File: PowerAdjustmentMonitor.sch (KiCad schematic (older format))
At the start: 37 parts, among them U3 LM317T, U4 LM317T, U5 LM337T, U6 LM337T

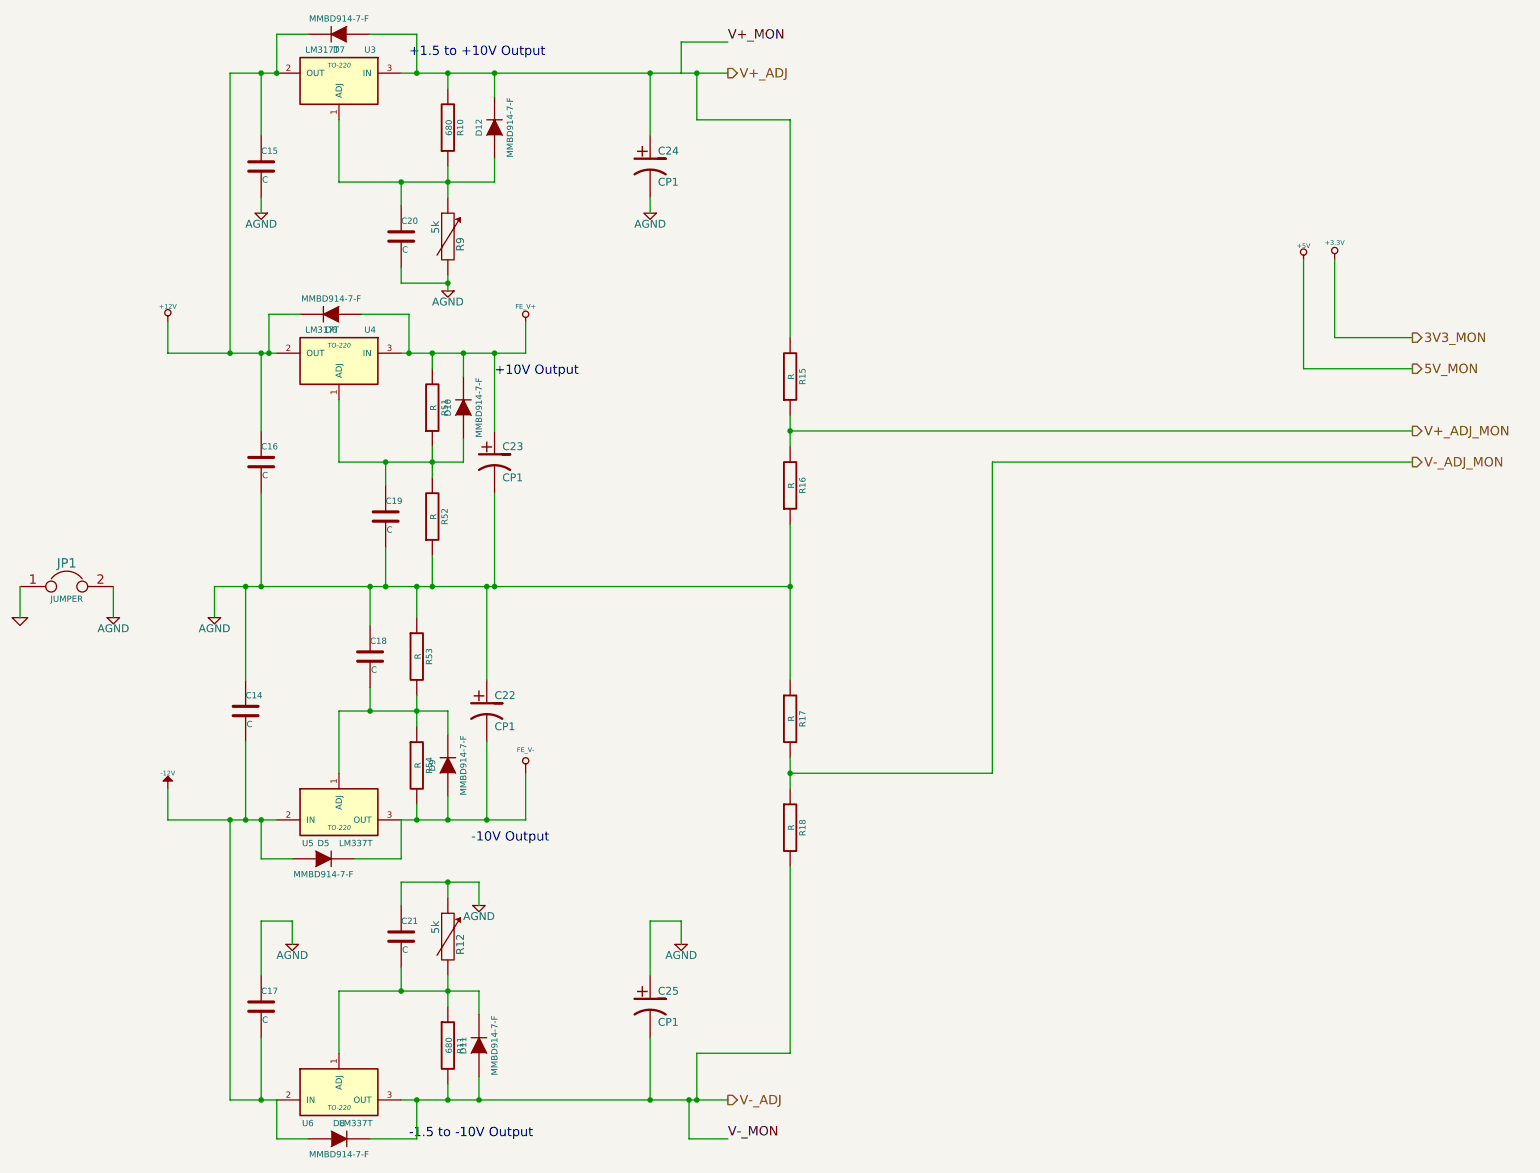
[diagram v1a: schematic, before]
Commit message: Updates from Layout Work Session 4 video
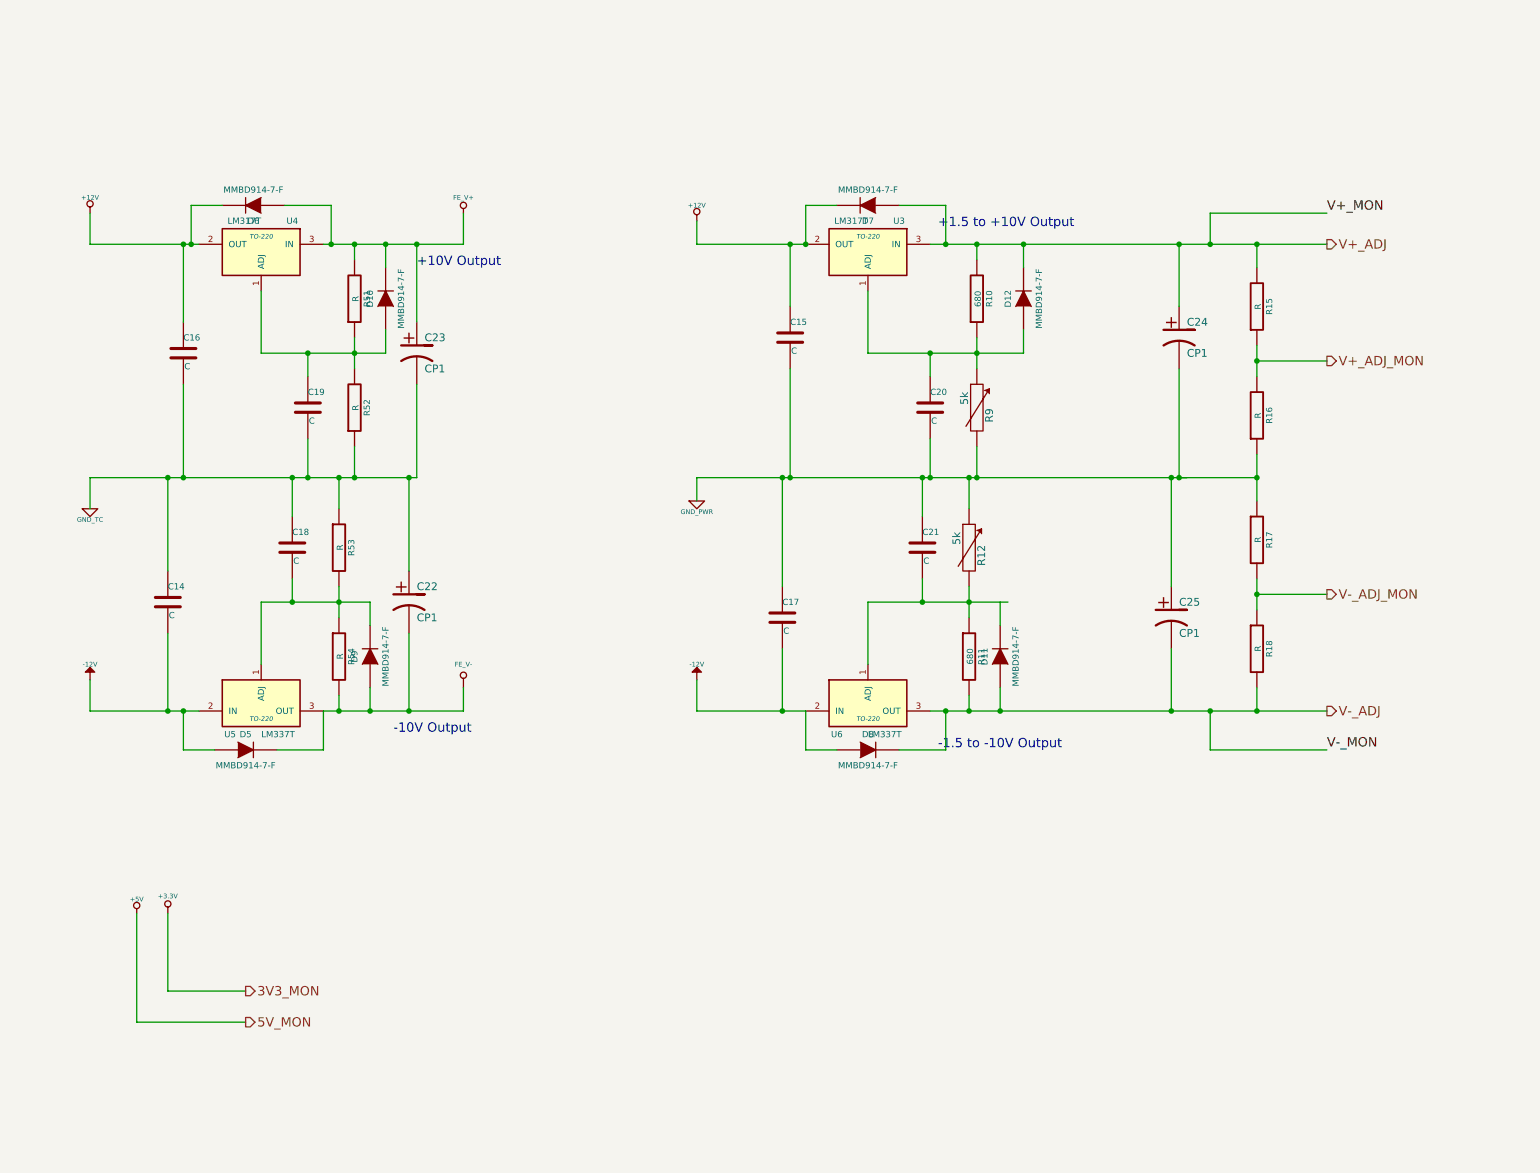
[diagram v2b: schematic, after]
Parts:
- removed JP1: JUMPER, symbol JUMPER
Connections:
- net at C21.2, R11.1, R12.2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: no longer D11.2 (K)
- net AGND renamed GND_PWR
- net GND_PWR: no longer C14.1, C16.2, C18.1, C19.2, C22.1, C23.2, R52.1, R53.1
- new net GND_TC: C14.1, C16.2, C18.1, C19.2, C22.1, C23.2, R52.1, R53.1
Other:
- moved on the sheet: C14, C15, C16, C17, C18, C19, C20, C21, C22, C23, C24, C25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

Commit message: Updates from Layout Work Session 5 video
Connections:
- net GND_TC renamed AGND
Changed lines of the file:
@@
 $EndDescr
 $Comp
-L +3.3V #PWR024
+L +3.3V #PWR025
 U 1 1 52F2A379
 P 2200 6200
-F 0 "#PWR024" H 2200 6160 30  0001 C CNN
+F 0 "#PWR025" H 2200 6160 30  0001 C CNN
 F 1 "+3.3V" H 2200 6310 30  0000 C CNN
 F 2 "" H 2200 6200 60  0000 C CNN
@@
 $EndComp
 $Comp
-L +5V #PWR025
+L +5V #PWR026
 U 1 1 52F2A37F
 P 2000 6200
-F 0 "#PWR025" H 2000 6290 20  0001 C CNN
+F 0 "#PWR026" H 2000 6290 20  0001 C CNN
 F 1 "+5V" H 2000 6290 30  0000 C CNN
 F 2 "" H 2000 6200 60  0000 C CNN
@@
 $EndComp
 $Comp
-L +12V #PWR026
+L +12V #PWR027
 U 1 1 52F2A40B
 P 1700 1700
-F 0 "#PWR026" H 1700 1650 20  0001 C CNN
+F 0 "#PWR027" H 1700 1650 20  0001 C CNN
 F 1 "+12V" H 1700 1800 30  0000 C CNN
 F 2 "" H 1700 1700 60  0000 C CNN
@@
 $EndComp
 $Comp
-L -12V #PWR027
+L -12V #PWR028
 U 1 1 52F2A411
 P 1700 4700
-F 0 "#PWR027" H 1700 4830 20  0001 C CNN
+F 0 "#PWR028" H 1700 4830 20  0001 C CNN
 F 1 "-12V" H 1700 4800 30  0000 C CNN
 F 2 "" H 1700 4700 60  0000 C CNN
@@
 $EndComp
 $Comp
-L FE_V+ #PWR028
+L FE_V+ #PWR029
 U 1 1 52F2A802
 P 4100 1700
-F 0 "#PWR028" H 4100 1800 30  0001 C CNN
+F 0 "#PWR029" H 4100 1800 30  0001 C CNN
 F 1 "FE_V+" H 4100 1800 30  0000 C CNN
 F 2 "" H 4100 1700 60  0000 C CNN
@@
 $EndComp
 $Comp
-L GND_PWR #PWR029
+L GND_PWR #PWR030
 U 1 1 53152874
 P 5600 3550
-F 0 "#PWR029" H 5600 3550 30  0001 C CNN
+F 0 "#PWR030" H 5600 3550 30  0001 C CNN
 F 1 "GND_PWR" H 5600 3480 30  0000 C CNN
 F 2 "" H 5600 3550 60  0000 C CNN
@@
 $EndComp
 $Comp
-L +12V #PWR030
+L +12V #PWR031
 U 1 1 5315289E
 P 5600 1750
-F 0 "#PWR030" H 5600 1700 20  0001 C CNN
+F 0 "#PWR031" H 5600 1700 20  0001 C CNN
 F 1 "+12V" H 5600 1850 30  0000 C CNN
 F 2 "" H 5600 1750 60  0000 C CNN
@@
 $EndComp
 $Comp
-L -12V #PWR031
+L -12V #PWR032
 U 1 1 53152B82
 P 5600 4700
-F 0 "#PWR031" H 5600 4830 20  0001 C CNN
+F 0 "#PWR032" H 5600 4830 20  0001 C CNN
 F 1 "-12V" H 5600 4800 30  0000 C CNN
 F 2 "" H 5600 4700 60  0000 C CNN
@@
 	1    0    0    -1
 $EndComp
-$Comp
-L GND_TC #PWR032
-U 1 1 53152BBD
-P 1700 3600
-F 0 "#PWR032" H 1700 3600 30  0001 C CNN
-F 1 "GND_TC" H 1700 3530 30  0000 C CNN
-F 2 "" H 1700 3600 60  0000 C CNN
-F 3 "" H 1700 3600 60  0000 C CNN
-	1    1700 3600
-	1    0    0    -1
-$EndComp
 Wire Wire Line
 	1700 4900 1700 4700
@@
 	3200 5150 3200 4900
 Wire Wire Line
-	2300 4900 2300 5150
+	2300 5150 2300 4900
 Connection ~ 2300 4900
 Wire Wire Line
@@
 	8700 3400 8700 2700
 Connection ~ 8700 3400
+$Comp
+L AGND #PWR033
+U 1 1 5316392A
+P 1700 3600
+F 0 "#PWR033" H 1700 3600 40  0001 C CNN
+F 1 "AGND" H 1700 3530 50  0000 C CNN
+F 2 "" H 1700 3600 60  0000 C CNN
+F 3 "" H 1700 3600 60  0000 C CNN
+	1    1700 3600
+	1    0    0    -1
+$EndComp
 $EndSCHEMATC

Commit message: Updates from Layout Work Session 6 video
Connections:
- net at C21.2, R11.1, R12.2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: now also D11.2 (K)
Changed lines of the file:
@@
 $EndDescr
 $Comp
-L +3.3V #PWR025
+L +3.3V #PWR028
 U 1 1 52F2A379
 P 2200 6200
-F 0 "#PWR025" H 2200 6160 30  0001 C CNN
+F 0 "#PWR028" H 2200 6160 30  0001 C CNN
 F 1 "+3.3V" H 2200 6310 30  0000 C CNN
 F 2 "" H 2200 6200 60  0000 C CNN
@@
 $EndComp
 $Comp
-L +5V #PWR026
+L +5V #PWR029
 U 1 1 52F2A37F
 P 2000 6200
-F 0 "#PWR026" H 2000 6290 20  0001 C CNN
+F 0 "#PWR029" H 2000 6290 20  0001 C CNN
 F 1 "+5V" H 2000 6290 30  0000 C CNN
 F 2 "" H 2000 6200 60  0000 C CNN
@@
 $EndComp
 $Comp
-L +12V #PWR027
+L +12V #PWR030
 U 1 1 52F2A40B
 P 1700 1700
-F 0 "#PWR027" H 1700 1650 20  0001 C CNN
+F 0 "#PWR030" H 1700 1650 20  0001 C CNN
 F 1 "+12V" H 1700 1800 30  0000 C CNN
 F 2 "" H 1700 1700 60  0000 C CNN
@@
 $EndComp
 $Comp
-L -12V #PWR028
+L -12V #PWR031
 U 1 1 52F2A411
 P 1700 4700
-F 0 "#PWR028" H 1700 4830 20  0001 C CNN
+F 0 "#PWR031" H 1700 4830 20  0001 C CNN
 F 1 "-12V" H 1700 4800 30  0000 C CNN
 F 2 "" H 1700 4700 60  0000 C CNN
@@
 $EndComp
 $Comp
-L FE_V+ #PWR029
+L FE_V+ #PWR032
 U 1 1 52F2A802
 P 4100 1700
-F 0 "#PWR029" H 4100 1800 30  0001 C CNN
+F 0 "#PWR032" H 4100 1800 30  0001 C CNN
 F 1 "FE_V+" H 4100 1800 30  0000 C CNN
 F 2 "" H 4100 1700 60  0000 C CNN
@@
 $EndComp
 $Comp
-L FE_V- #PWR36
+L FE_V- #PWR37
 U 1 1 530BD9FD
 P 4100 4750
-F 0 "#PWR36" H 4100 4950 40  0001 C CNN
+F 0 "#PWR37" H 4100 4950 40  0001 C CNN
 F 1 "FE_V-" H 4100 4900 30  0000 C CNN
 F 2 "" H 4100 4750 60  0000 C CNN
@@
 $EndComp
 $Comp
-L GND_PWR #PWR030
+L GND_PWR #PWR033
 U 1 1 53152874
 P 5600 3550
-F 0 "#PWR030" H 5600 3550 30  0001 C CNN
+F 0 "#PWR033" H 5600 3550 30  0001 C CNN
 F 1 "GND_PWR" H 5600 3480 30  0000 C CNN
 F 2 "" H 5600 3550 60  0000 C CNN
@@
 $EndComp
 $Comp
-L +12V #PWR031
+L +12V #PWR034
 U 1 1 5315289E
 P 5600 1750
-F 0 "#PWR031" H 5600 1700 20  0001 C CNN
+F 0 "#PWR034" H 5600 1700 20  0001 C CNN
 F 1 "+12V" H 5600 1850 30  0000 C CNN
 F 2 "" H 5600 1750 60  0000 C CNN
@@
 $EndComp
 $Comp
-L -12V #PWR032
+L -12V #PWR035
 U 1 1 53152B82
 P 5600 4700
-F 0 "#PWR032" H 5600 4830 20  0001 C CNN
+F 0 "#PWR035" H 5600 4830 20  0001 C CNN
 F 1 "-12V" H 5600 4800 30  0000 C CNN
 F 2 "" H 5600 4700 60  0000 C CNN
@@
 	1700 3400 1700 3600
 Wire Wire Line
-	6700 4200 7600 4200
-Wire Wire Line
 	6700 4200 6700 4600
 Connection ~ 7350 4200
@@
 Connection ~ 8700 3400
 $Comp
-L AGND #PWR033
+L AGND #PWR036
 U 1 1 5316392A
 P 1700 3600
-F 0 "#PWR033" H 1700 3600 40  0001 C CNN
+F 0 "#PWR036" H 1700 3600 40  0001 C CNN
 F 1 "AGND" H 1700 3530 50  0000 C CNN
 F 2 "" H 1700 3600 60  0000 C CNN
@@
 	1    0    0    -1
 $EndComp
+Wire Wire Line
+	6700 4200 7550 4200
 $EndSCHEMATC

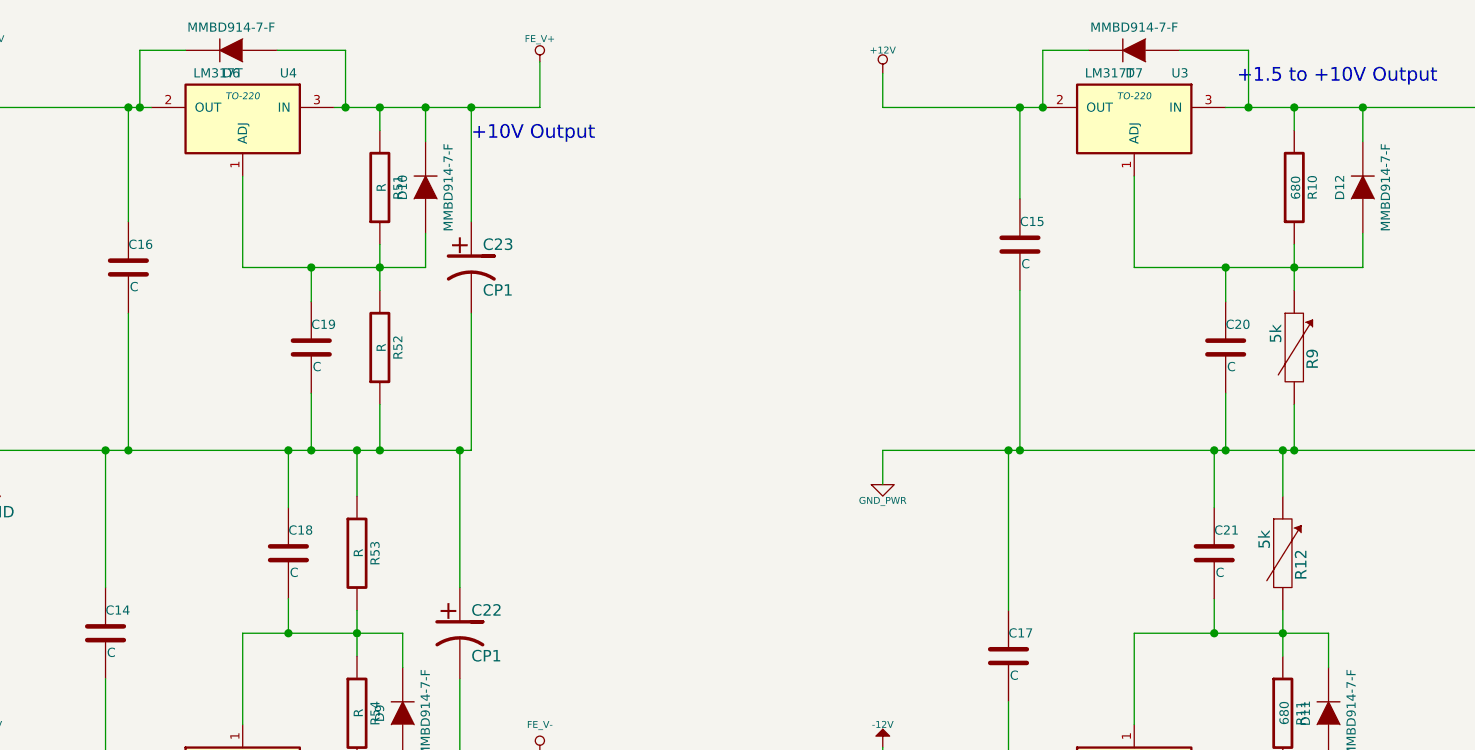
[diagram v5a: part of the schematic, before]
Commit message: Power output layout
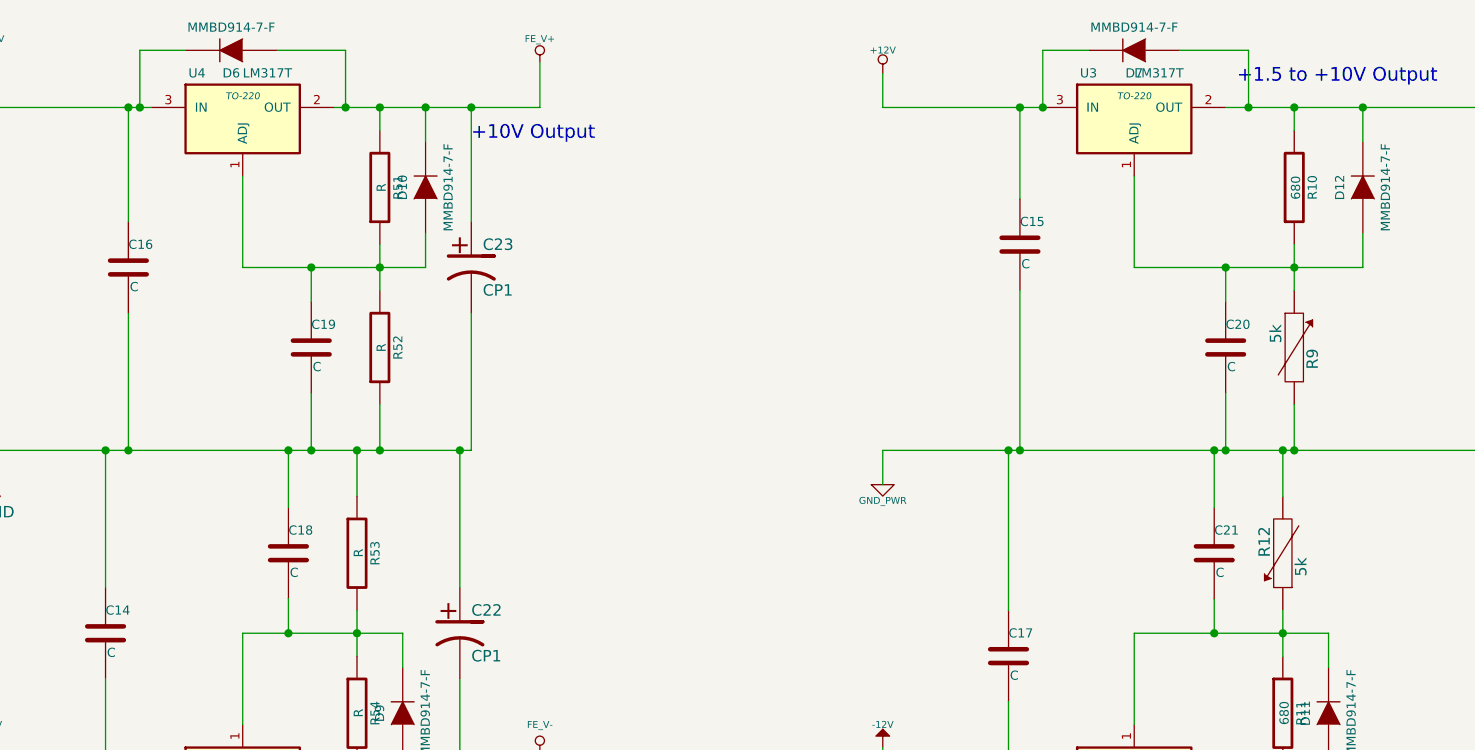
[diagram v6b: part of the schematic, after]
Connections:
- net +12V: now also U3.3 (IN), U4.3 (IN); no longer U3.2 (OUT), U4.2 (OUT)
- net FE_V+: now also U4.2 (OUT); no longer U4.3 (IN)
- net GND_PWR: now also R12.2; no longer R12.1
- net V+_ADJ: now also U3.2 (OUT); no longer U3.3 (IN)
- net at C21.2, D11.2 (K), R11.1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: now also R12.1; no longer R12.2
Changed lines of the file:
@@
 $EndDescr
 $Comp
-L +3.3V #PWR35
+L +3.3V #PWR027
 U 1 1 52F2A379
 P 2200 6200
-F 0 "#PWR35" H 2200 6160 30  0001 C CNN
+F 0 "#PWR027" H 2200 6160 30  0001 C CNN
 F 1 "+3.3V" H 2200 6310 30  0000 C CNN
 F 2 "" H 2200 6200 60  0000 C CNN
@@
 $EndComp
 $Comp
-L +5V #PWR34
+L +5V #PWR028
 U 1 1 52F2A37F
 P 2000 6200
-F 0 "#PWR34" H 2000 6290 20  0001 C CNN
+F 0 "#PWR028" H 2000 6290 20  0001 C CNN
 F 1 "+5V" H 2000 6290 30  0000 C CNN
 F 2 "" H 2000 6200 60  0000 C CNN
@@
 $EndComp
 $Comp
-L +12V #PWR31
+L +12V #PWR029
 U 1 1 52F2A40B
 P 1700 1700
-F 0 "#PWR31" H 1700 1650 20  0001 C CNN
+F 0 "#PWR029" H 1700 1650 20  0001 C CNN
 F 1 "+12V" H 1700 1800 30  0000 C CNN
 F 2 "" H 1700 1700 60  0000 C CNN
@@
 $EndComp
 $Comp
-L -12V #PWR33
+L -12V #PWR030
 U 1 1 52F2A411
 P 1700 4700
-F 0 "#PWR33" H 1700 4830 20  0001 C CNN
+F 0 "#PWR030" H 1700 4830 20  0001 C CNN
 F 1 "-12V" H 1700 4800 30  0000 C CNN
 F 2 "" H 1700 4700 60  0000 C CNN
@@
 $EndComp
 $Comp
-L FE_V+ #PWR36
+L FE_V+ #PWR031
 U 1 1 52F2A802
 P 4100 1700
-F 0 "#PWR36" H 4100 1800 30  0001 C CNN
+F 0 "#PWR031" H 4100 1800 30  0001 C CNN
 F 1 "FE_V+" H 4100 1800 30  0000 C CNN
 F 2 "" H 4100 1700 60  0000 C CNN
@@
 F 3 "" H 6700 1950 60  0000 C CNN
 	1    6700 1950
-	-1   0    0    -1
+	1    0    0    -1
 $EndComp
 $Comp
@@
 F 3 "" H 7350 3850 60  0000 C CNN
 	1    7350 3850
-	1    0    0    -1
+	-1   0    0    1
 $EndComp
 $Comp
@@
 F 3 "" H 2800 1950 60  0000 C CNN
 	1    2800 1950
-	-1   0    0    -1
+	1    0    0    -1
 $EndComp
 $Comp
@@
 $EndComp
 $Comp
-L GND_PWR #PWR39
+L GND_PWR #PWR032
 U 1 1 53152874
 P 5600 3550
-F 0 "#PWR39" H 5600 3550 30  0001 C CNN
+F 0 "#PWR032" H 5600 3550 30  0001 C CNN
 F 1 "GND_PWR" H 5600 3480 30  0000 C CNN
 F 2 "" H 5600 3550 60  0000 C CNN
@@
 $EndComp
 $Comp
-L +12V #PWR38
+L +12V #PWR033
 U 1 1 5315289E
 P 5600 1750
-F 0 "#PWR38" H 5600 1700 20  0001 C CNN
+F 0 "#PWR033" H 5600 1700 20  0001 C CNN
 F 1 "+12V" H 5600 1850 30  0000 C CNN
 F 2 "" H 5600 1750 60  0000 C CNN
@@
 $EndComp
 $Comp
-L -12V #PWR40
+L -12V #PWR034
 U 1 1 53152B82
 P 5600 4700
-F 0 "#PWR40" H 5600 4830 20  0001 C CNN
+F 0 "#PWR034" H 5600 4830 20  0001 C CNN
 F 1 "-12V" H 5600 4800 30  0000 C CNN
 F 2 "" H 5600 4700 60  0000 C CNN
@@
 Connection ~ 8700 3400
 $Comp
-L AGND #PWR32
+L AGND #PWR035
 U 1 1 5316392A
 P 1700 3600
-F 0 "#PWR32" H 1700 3600 40  0001 C CNN
+F 0 "#PWR035" H 1700 3600 40  0001 C CNN
 F 1 "AGND" H 1700 3530 50  0000 C CNN
 F 2 "" H 1700 3600 60  0000 C CNN
